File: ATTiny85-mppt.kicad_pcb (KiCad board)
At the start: 2 copper layers, 97.6 x 90.8 mm, 55 parts, among them Q1 BUK9511-55A127, Q2 BUK9511-55A127, Q3 2N2222A, Q4 2N2222A, Q5 2N2904A, Q6 BUK9508-55A, U1 LM7805_TO220, U2 LM358N, U3 ATtiny85-20PU

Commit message: Update PCB layout.
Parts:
- renumbered Q6 to Q6(ALT), R17 to R17(ALT)
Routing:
- net Net-(R16-Pad1): track 83.7 -> 74.1 mm
- net Net-(C6-Pad1): track 36.3 -> 31.8 mm
- net /PV-Current: track 37.0 -> 33.9 mm
- net Net-(R13-Pad2): track 32.2 -> 29.8 mm
- net Net-(R3-Pad1): track 30.5 -> 31.6 mm
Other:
- board text added: "MPPT 1.4"
- board text removed: "MPPT 1.1"
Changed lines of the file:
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@@
     (thickness 1.6)
     (drawings 7)
-    (tracks 309)
+    (tracks 305)
     (zones 0)
     (modules 55)
@@
   )
   (setup
-    (last_trace_width 1.5)
+    (last_trace_width 0.25)
     (user_trace_width 0.5)
     (user_trace_width 1)
@@
     (descr https://www.omron.com/ecb/products/pdf/en-b3f.pdf)
     (tags "tact sw push 6mm")
-    (fp_text reference "CAL @ Reset" (at 2.89052 -3.41884 90) (layer F.SilkS)
+    (fp_text reference "CAL @ Reset" (at 9.33196 2.47904 180) (layer F.SilkS)
       (effects (font (size 1 1) (thickness 0.15)))
     )
@@
     (descr "TO-220, Neutral, Vertical,")
     (tags "TO-220, Neutral, Vertical,")
-    (fp_text reference Q6 (at -6.82244 -0.3302) (layer F.SilkS)
+    (fp_text reference "Q6(ALT)" (at -6.82244 -0.3302) (layer F.SilkS)
       (effects (font (size 1 1) (thickness 0.15)))
     )
@@
     (descr "Resistor, Axial_DIN0309 series, Axial, Horizontal, pin pitch=12.7mm, 0.5W = 1/2W, length*diameter=9*3.2mm^2, http://cdn-reichelt.de/documents/datenblatt/B400/1_4W%23YAG.pdf")
     (tags "Resistor Axial_DIN0309 series Axial Horizontal pin pitch 12.7mm 0.5W = 1/2W length 9mm diameter 3.2mm")
-    (fp_text reference R17 (at 7.46252 0.62992) (layer F.SilkS)
+    (fp_text reference "R17(ALT)" (at 7.46252 0.62992) (layer F.SilkS)
       (effects (font (size 1 1) (thickness 0.15)))
     )
@@
     (effects (font (size 1.5 1.5) (thickness 0.3)))
   )
-  (gr_text "MPPT 1.1" (at 71.99884 110.81512) (layer F.SilkS)
+  (gr_text "MPPT 1.4" (at 58.12028 77.02296) (layer F.SilkS)
     (effects (font (size 1.5 1.5) (thickness 0.3)))
   )
@@
   (segment (start 63.64732 64.29248) (end 70.91172 57.02808) (width 2) (layer B.Cu) (net 8))
   (segment (start 62.8142 64.29248) (end 63.64732 64.29248) (width 2) (layer B.Cu) (net 8))
-  (segment (start 88.25484 54.01564) (end 90.3732 54.01564) (width 1.5) (layer F.Cu) (net 8))
-  (segment (start 72.04309 57.02808) (end 75.00473 59.98972) (width 1.5) (layer F.Cu) (net 8))
-  (segment (start 75.00473 59.98972) (end 85.68436 59.98972) (width 1.5) (layer F.Cu) (net 8))
-  (segment (start 85.68436 59.98972) (end 87.65032 58.02376) (width 1.5) (layer F.Cu) (net 8))
-  (segment (start 70.91172 57.02808) (end 72.04309 57.02808) (width 1.5) (layer F.Cu) (net 8))
-  (segment (start 87.65032 58.02376) (end 87.65032 54.62016) (width 1.5) (layer F.Cu) (net 8))
-  (segment (start 87.65032 54.62016) (end 88.25484 54.01564) (width 1.5) (layer F.Cu) (net 8))
+  (segment (start 71.711719 56.228081) (end 80.124199 56.228081) (width 1.2) (layer F.Cu) (net 8))
+  (segment (start 70.91172 57.02808) (end 71.711719 56.228081) (width 1.2) (layer F.Cu) (net 8))
+  (segment (start 82.33664 54.01564) (end 90.3732 54.01564) (width 1.2) (layer F.Cu) (net 8))
+  (segment (start 80.124199 56.228081) (end 82.33664 54.01564) (width 1.2) (layer F.Cu) (net 8))
   (segment (start 70.33768 34.11728) (end 70.33768 27.5844) (width 3) (layer B.Cu) (net 9))
   (segment (start 78.60284 27.5844) (end 79.6036 28.58516) (width 3) (layer B.Cu) (net 9))
@@
   (segment (start 78.17104 76.76388) (end 88.10244 66.83248) (width 1.5) (layer F.Cu) (net 18))
   (segment (start 78.67396 81.2546) (end 83.74888 81.2546) (width 1.5) (layer B.Cu) (net 19))
-  (segment (start 97.917 73.04385) (end 97.91192 73.04893) (width 1.2) (layer F.Cu) (net 19))
-  (segment (start 97.917 71.91248) (end 97.917 73.04385) (width 1.2) (layer F.Cu) (net 19))
-  (segment (start 97.91192 73.04893) (end 97.91192 81.69656) (width 1.2) (layer F.Cu) (net 19))
-  (segment (start 83.52028 81.2546) (end 87.32012 85.05444) (width 1.2) (layer F.Cu) (net 19))
-  (segment (start 94.55404 85.05444) (end 97.91192 81.69656) (width 1.2) (layer F.Cu) (net 19))
-  (segment (start 87.32012 85.05444) (end 94.55404 85.05444) (width 1.2) (layer F.Cu) (net 19))
+  (segment (start 97.917 71.91248) (end 97.917 80.61452) (width 1.2) (layer F.Cu) (net 19))
+  (segment (start 97.917 80.61452) (end 95.61576 82.91576) (width 1.2) (layer F.Cu) (net 19))
+  (segment (start 85.18144 82.91576) (end 83.52028 81.2546) (width 1.2) (layer F.Cu) (net 19))
+  (segment (start 95.61576 82.91576) (end 85.18144 82.91576) (width 1.2) (layer F.Cu) (net 19))
   (segment (start 95.123 91.8972) (end 95.13824 91.88196) (width 2) (layer B.Cu) (net 20))
   (segment (start 90.297 91.8972) (end 95.123 91.8972) (width 2) (layer B.Cu) (net 20))
-  (segment (start 97.917 69.37248) (end 100.29952 71.755) (width 1.2) (layer F.Cu) (net 20))
-  (segment (start 100.29952 71.755) (end 100.29952 86.72068) (width 1.2) (layer F.Cu) (net 20))
-  (segment (start 100.29952 86.72068) (end 95.13824 91.88196) (width 1.2) (layer F.Cu) (net 20))
+  (segment (start 97.917 69.37248) (end 99.80168 69.37248) (width 1.2) (layer F.Cu) (net 20))
+  (segment (start 99.80168 69.37248) (end 100.28428 69.85508) (width 1.2) (layer F.Cu) (net 20))
+  (segment (start 100.28428 69.85508) (end 100.28428 82.16392) (width 1.2) (layer F.Cu) (net 20))
+  (segment (start 95.13824 87.30996) (end 95.13824 91.88196) (width 1.2) (layer F.Cu) (net 20))
+  (segment (start 100.28428 82.16392) (end 95.13824 87.30996) (width 1.2) (layer F.Cu) (net 20))
   (segment (start 96.78563 66.83248) (end 97.917 66.83248) (width 2) (layer B.Cu) (net 21))
   (segment (start 93.96837 66.83248) (end 96.78563 66.83248) (width 2) (layer B.Cu) (net 21))
@@
   (segment (start 66.81216 76.6318) (end 66.81216 81.18856) (width 1.5) (layer F.Cu) (net 23))
   (segment (start 69.55536 73.8886) (end 66.81216 76.6318) (width 1.5) (layer F.Cu) (net 23))
-  (segment (start 85.36285 76.76388) (end 85.36793 76.7588) (width 1.2) (layer F.Cu) (net 24))
-  (segment (start 84.23148 76.76388) (end 85.36285 76.76388) (width 1.2) (layer F.Cu) (net 24))
-  (segment (start 85.36793 76.7588) (end 93.30944 76.7588) (width 1.2) (layer F.Cu) (net 24))
-  (segment (start 93.30944 76.7588) (end 95.26524 74.803) (width 1.2) (layer F.Cu) (net 24))
-  (segment (start 95.26524 74.803) (end 95.26524 65.41516) (width 1.2) (layer F.Cu) (net 24))
   (segment (start 94.14256 64.29248) (end 90.297 64.29248) (width 1.2) (layer F.Cu) (net 24))
-  (segment (start 95.26524 65.41516) (end 94.14256 64.29248) (width 1.2) (layer F.Cu) (net 24))
   (segment (start 98.22688 60.20816) (end 102.82936 60.20816) (width 1.5) (layer F.Cu) (net 24))
   (segment (start 94.14256 64.29248) (end 98.22688 60.20816) (width 1.5) (layer F.Cu) (net 24))
+  (segment (start 85.36285 76.76388) (end 86.83605 75.29068) (width 1.2) (layer F.Cu) (net 24))
+  (segment (start 84.23148 76.76388) (end 85.36285 76.76388) (width 1.2) (layer F.Cu) (net 24))
+  (segment (start 86.83605 75.29068) (end 90.95232 75.29068) (width 1.2) (layer F.Cu) (net 24))
+  (segment (start 94.14256 72.10044) (end 94.14256 64.29248) (width 1.2) (layer F.Cu) (net 24))
+  (segment (start 90.95232 75.29068) (end 94.14256 72.10044) (width 1.2) (layer F.Cu) (net 24))
   (segment (start 60.29364 97.31488) (end 60.29364 103.81488) (width 3) (layer B.Cu) (net 25))
   (segment (start 88.0732 48.93564) (end 90.3732 48.93564) (width 1.5) (layer B.Cu) (net 25))
   (segment (start 84.81568 52.19316) (end 88.0732 48.93564) (width 1.5) (layer B.Cu) (net 25))
   (segment (start 84.81568 56.55056) (end 84.81568 52.19316) (width 1.5) (layer B.Cu) (net 25))
-  (segment (start 60.29364 97.31488) (end 60.29364 71.89636) (width 1.5) (layer F.Cu) (net 25))
-  (segment (start 60.29364 71.89636) (end 59.27852 70.88124) (width 1.5) (layer F.Cu) (net 25))
-  (segment (start 59.27852 70.88124) (end 59.27852 61.34608) (width 1.5) (layer F.Cu) (net 25))
-  (segment (start 59.27852 61.34608) (end 66.46672 54.15788) (width 1.5) (layer F.Cu) (net 25))
-  (segment (start 82.423 54.15788) (end 84.81568 56.55056) (width 1.5) (layer F.Cu) (net 25))
-  (segment (start 66.46672 54.15788) (end 82.423 54.15788) (width 1.5) (layer F.Cu) (net 25))
+  (segment (start 84.81568 56.55056) (end 81.65592 59.71032) (width 1.2) (layer F.Cu) (net 25))
+  (segment (start 81.65592 59.71032) (end 72.45096 59.71032) (width 1.2) (layer F.Cu) (net 25))
+  (segment (start 60.29364 95.900667) (end 60.29364 97.31488) (width 1.2) (layer F.Cu) (net 25))
+  (segment (start 60.29364 78.96948) (end 60.29364 95.900667) (width 1.2) (layer F.Cu) (net 25))
+  (segment (start 72.45096 66.81216) (end 60.29364 78.96948) (width 1.2) (layer F.Cu) (net 25))
+  (segment (start 72.45096 59.71032) (end 72.45096 66.81216) (width 1.2) (layer F.Cu) (net 25))
   (segment (start 104.874442 39.02964) (end 105.052242 38.85184) (width 1.5) (layer B.Cu) (net 26))
   (segment (start 103.79964 39.02964) (end 104.874442 39.02964) (width 1.5) (layer B.Cu) (net 26))

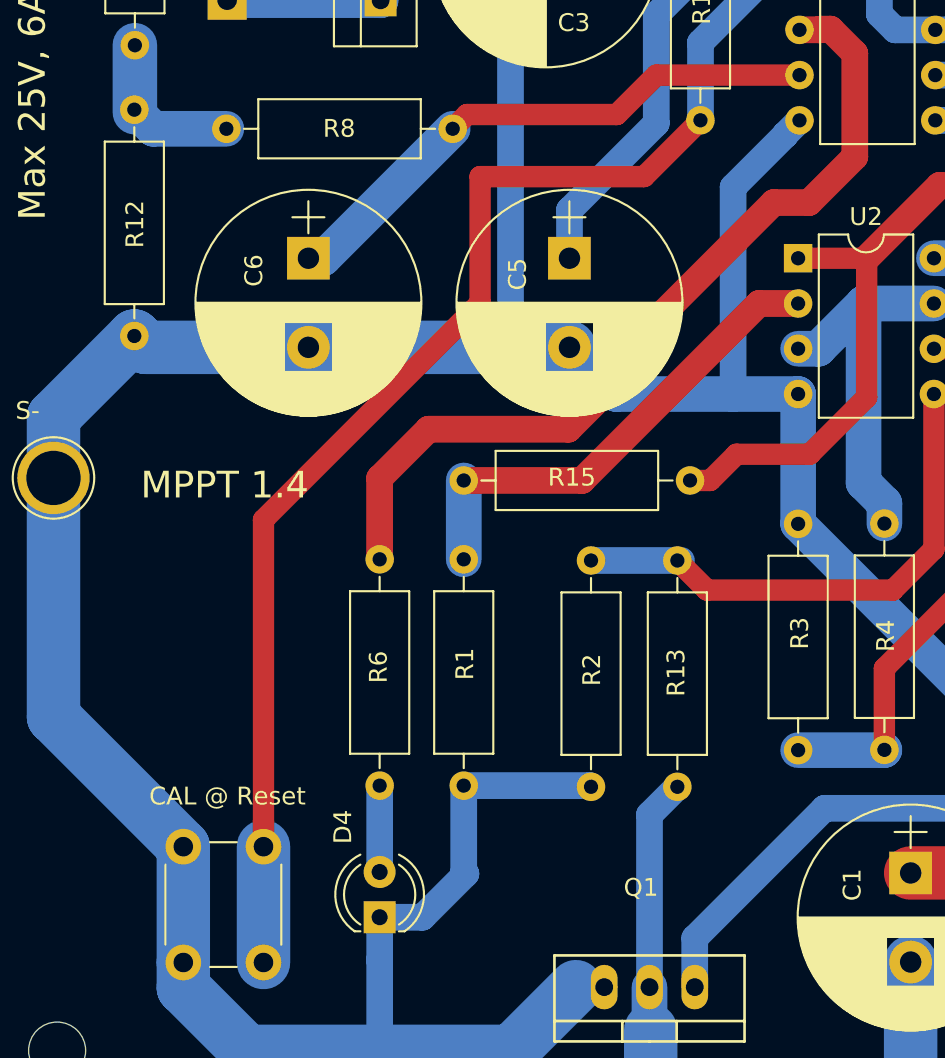
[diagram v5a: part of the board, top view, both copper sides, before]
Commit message: Add AREF capacitor.
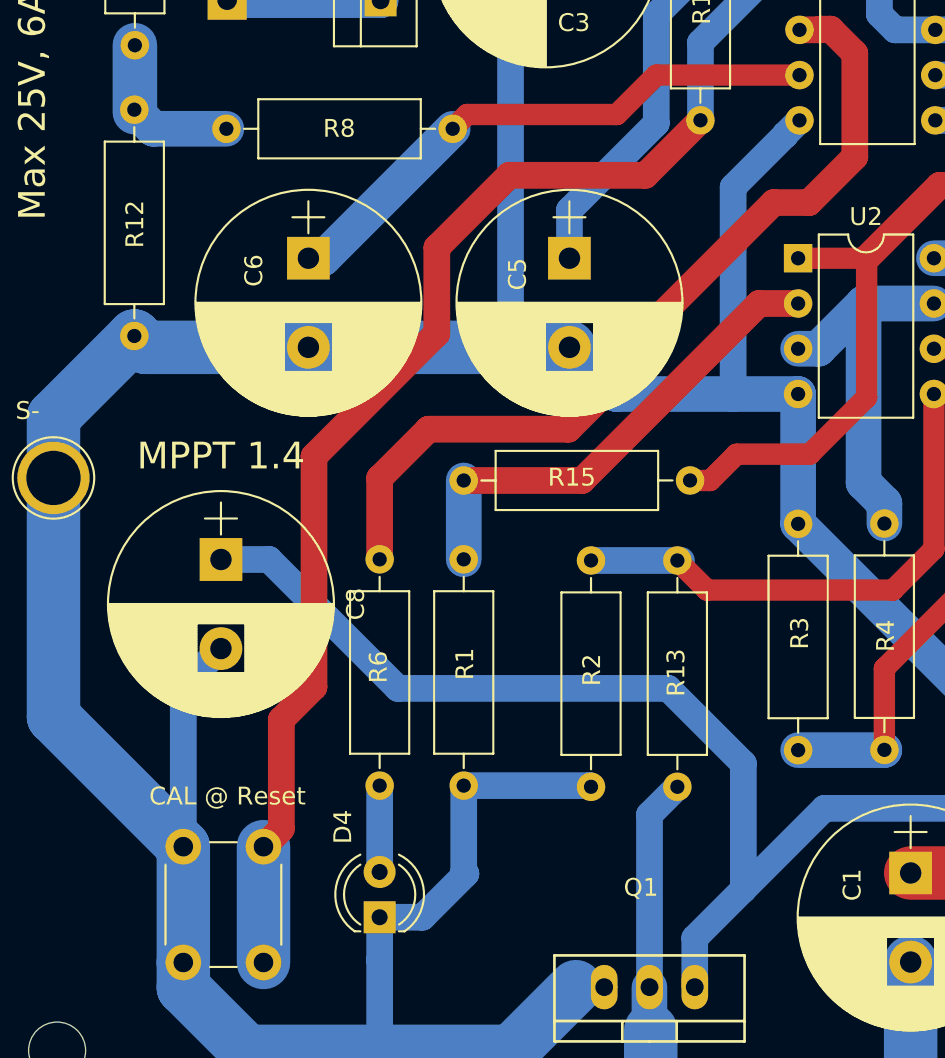
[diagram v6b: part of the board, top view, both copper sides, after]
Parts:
- added C8: 10u, Capacitors_THT:CP_Radial_D12.5mm_P5.00mm, F.Cu at (57.9, 81.2)
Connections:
- C5 pad 1: Net-(C5-Pad1) -> /PV-Current
- R11 pad 1: /PV-Current -> Net-(R11-Pad1)
- R11 pad 2: Net-(C5-Pad1) -> /PV-Current
- R15 pad 2: /PV-Current -> Net-(R11-Pad1)
- U2 pad 1: /PV-Current -> Net-(R11-Pad1)
- U3 pad 7: Net-(C5-Pad1) -> /PV-Current
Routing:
- net Net-(C5-Pad1): track 42.9 -> 0.00 mm
- net /3.6v: track 76.7 -> 117.9 mm
- net Net-(R11-Pad1): track 0.00 -> 33.9 mm
- net GND: track 259.0 -> 271.0 mm
- net /PV-Current: track 33.9 -> 42.9 mm
- net Net-(R16-Pad1): track 74.1 -> 73.2 mm

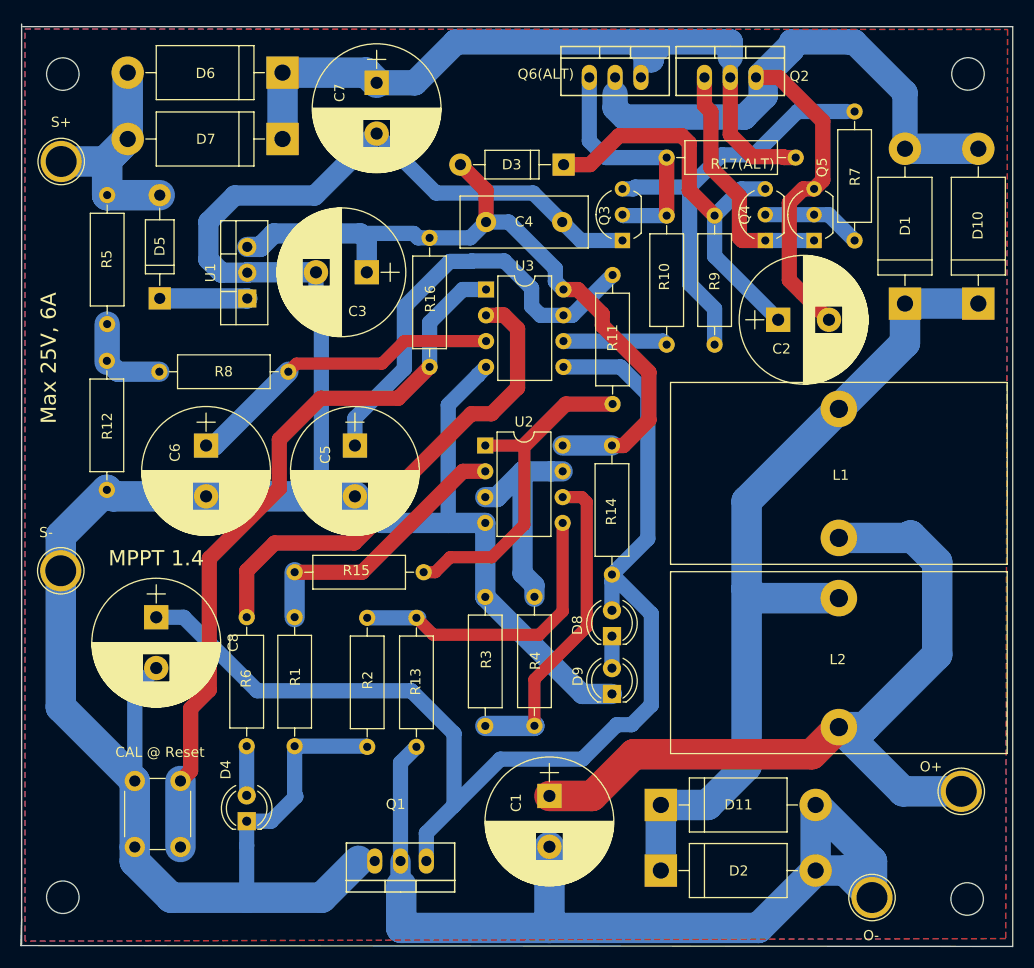
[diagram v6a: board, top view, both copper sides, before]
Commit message: remove some component.
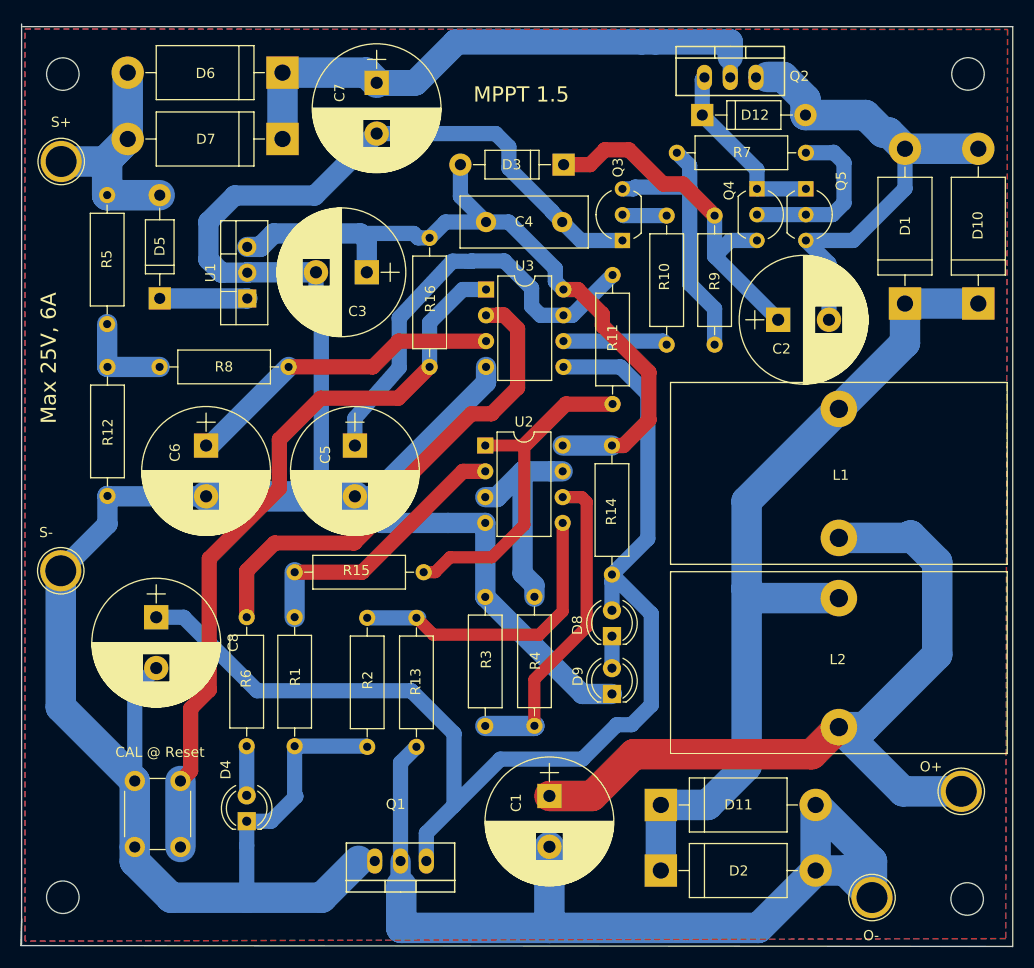
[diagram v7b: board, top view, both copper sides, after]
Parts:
- removed Q6(ALT): BUK9508-55A, TO_SOT_Packages_THT-2:TO-220_Neutral123_Vertical
- removed R17(ALT): 1M, Resistors_THT:R_Axial_DIN0309_L9.0mm_D3.2mm_P12.70mm_Horizontal
- added D12: BZX 55c12(12V), Diodes_THT:D_DO-41_SOD81_P10.16mm_Horizontal, F.Cu at (111.7, 31.8)
- moved R7 9.88 mm to (121.9, 35.5), turned to 180 degrees
- moved Q4 5.15 mm to (117.0, 39.0), turned to 270 degrees
- moved Q5 5.15 mm to (121.9, 39.0), turned to 270 degrees
- moved R12 0.60 mm to (53.1, 56.6)
- moved R8 0.47 mm to (58.2, 56.6)
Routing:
- net Net-(C2-Pad2): track 93.2 -> 50.8 mm
- net Net-(Q3-Pad2): track 24.7 -> 4.39 mm
- net Net-(C7-Pad1): track 103.5 -> 84.3 mm
- net Net-(Q3-Pad3): track 41.8 -> 27.1 mm
- net Net-(Q4-Pad2): track 9.85 -> 17.2 mm
- net Net-(D12-Pad1): track 24.7 -> 18.1 mm
- net Net-(C2-Pad1): track 40.9 -> 35.8 mm
- net GND: track 271.0 -> 273.6 mm
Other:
- board text added: "MPPT 1.5"
- board text removed: "MPPT 1.4"

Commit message: update PCB file. update capacitor and add resistor.
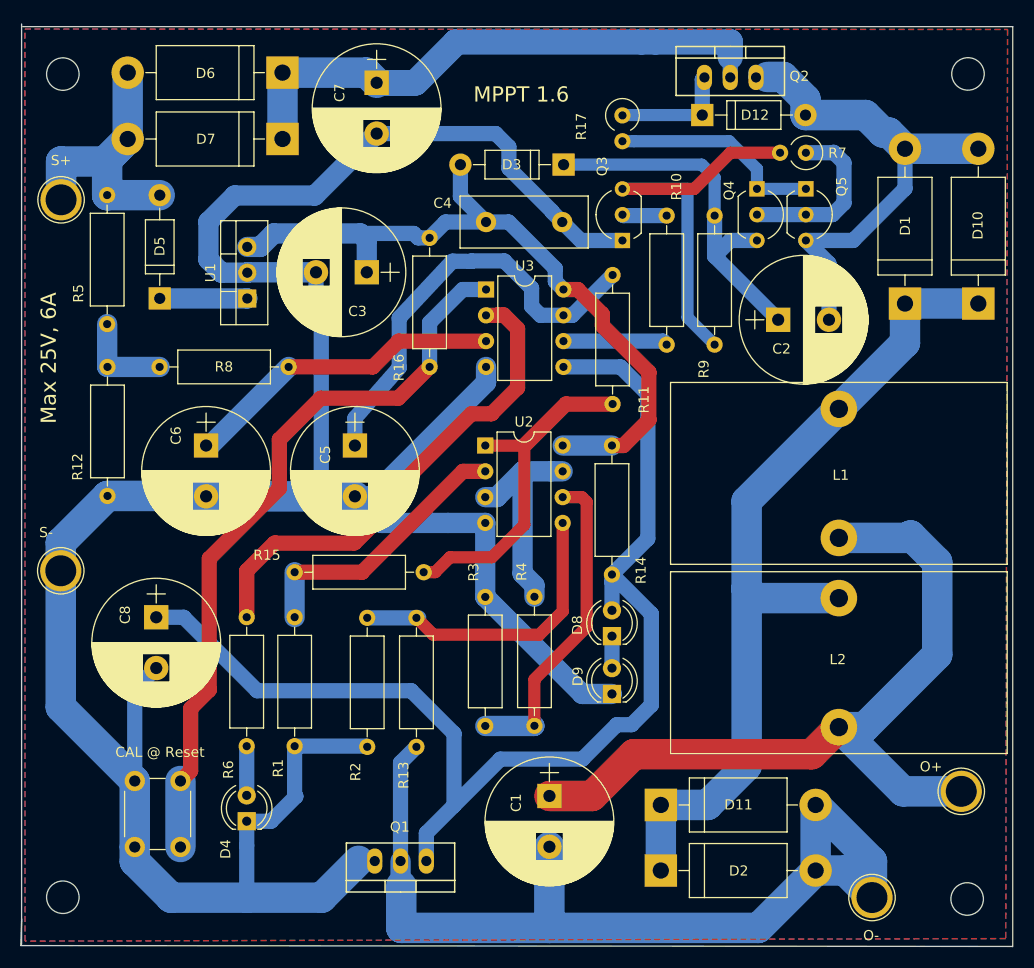
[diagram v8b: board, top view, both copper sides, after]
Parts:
- added R17: 1k, Resistors_THT:R_Axial_DIN0309_L9.0mm_D3.2mm_P2.54mm_Vertical, F.Cu at (103.8, 31.8)
- C2: value >10uF -> 47uF 50v
- R7: footprint Resistors_THT:R_Axial_DIN0309_L9.0mm_D3.2mm_P12.70mm_Horizontal -> Resistors_THT:R_Axial_DIN0309_L9.0mm_D3.2mm_P2.54mm_Vertical
- moved S+ 3.77 mm to (48.5, 40.1)
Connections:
- net Net-(R10-Pad1) renamed /~PWM
- Q4 pad 1: Net-(D12-Pad1) -> Net-(Q4-Pad1)
- Q5 pad 1: Net-(D12-Pad1) -> Net-(Q4-Pad1)
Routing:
- net Net-(Q4-Pad1): track 0.00 -> 21.1 mm
- net Net-(Q3-Pad3): track 27.1 -> 39.8 mm
- net Net-(D12-Pad1): track 18.1 -> 11.7 mm
- net +24V: track 25.5 -> 29.3 mm
- net Net-(C2-Pad1): track 35.8 -> 36.8 mm
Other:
- board text added: "MPPT 1.6"
- board text removed: "MPPT 1.5"
